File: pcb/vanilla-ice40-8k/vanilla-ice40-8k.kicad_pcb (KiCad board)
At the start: 6 copper layers, 50 x 50 mm, 129 parts, among them J10 Conn_01x05_Pin, J11 QSH-060-01-L-D-A, J12 QSH-060-01-L-D-A, J6 Conn_01x02_Pin, J7 Conn_01x02_Pin, J8 Conn_01x02_Pin, J9 Conn_01x06_Pin, Q1 DMG2305UX-13, U1 ICE40HX8K-CT256, U2 W25X40CLSN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

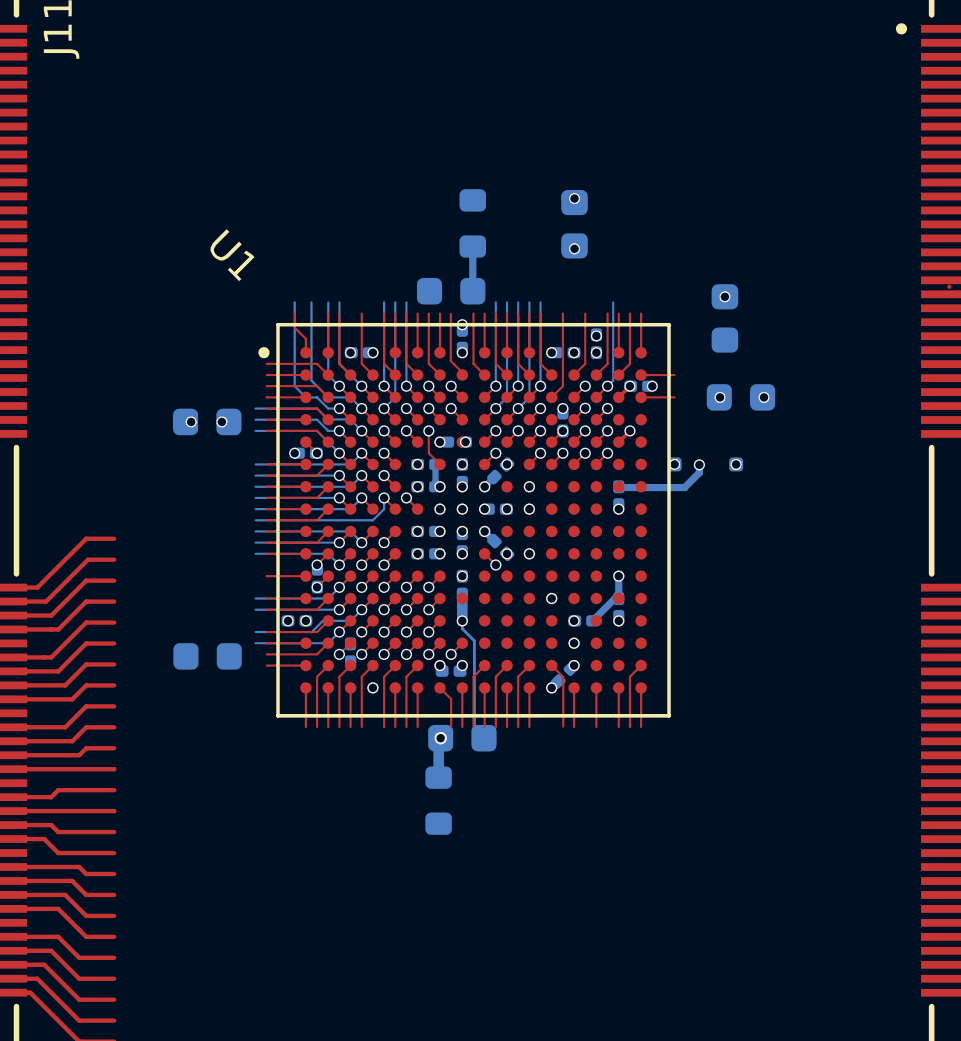
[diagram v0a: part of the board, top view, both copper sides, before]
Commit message: [pcb][hx8k] new IOR escape
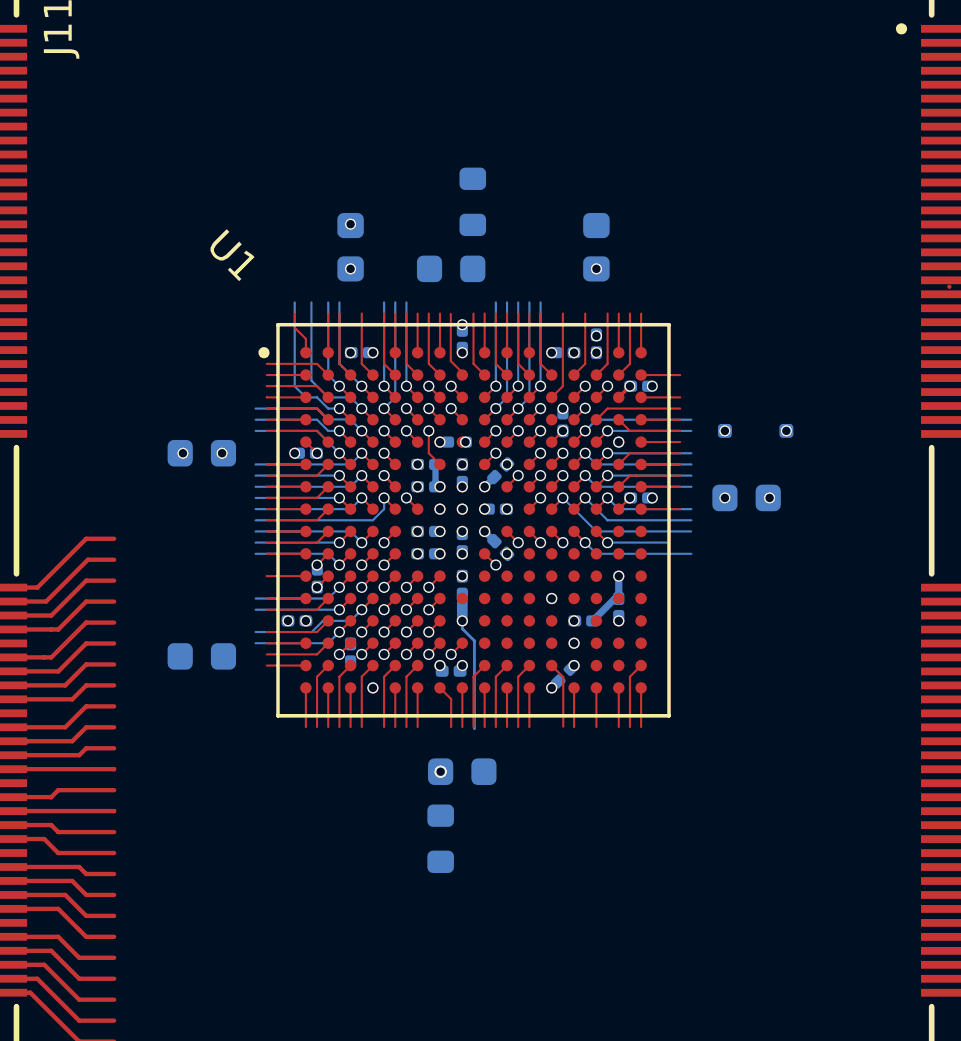
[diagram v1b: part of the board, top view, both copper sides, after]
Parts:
- moved C20 8.06 mm to (113.3, 105.4)
- moved C2 5.26 mm to (122.1, 105.4)
- moved C30 3.61 mm to (127.4, 114.4)
- moved D1 2.16 mm to (127.8, 112.0)
- moved R10 1.36 mm to (116.5, 126.6)
- moved C10 1.20 mm to (117.3, 124.2)
- moved C25 1.14 mm to (107.9, 112.8)
- moved C12 0.80 mm to (116.9, 106.2)
- moved R11 0.77 mm to (117.6, 103.8)
- moved C33 0.75 mm to (123.6, 114.4), turned to 0 degrees
- moved C15 0.21 mm to (107.9, 120.0)
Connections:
- U1 pad K11: unconnected-(U1C-IOB_103_CBSEL0-PadK11) -> /IOB_103_CBSEL0
- U1 pad P13: unconnected-(U1C-IOB_104_CBSEL1-PadP13) -> /IOB_103_CBSEL1
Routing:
- net /IOR_146_SCL: track 36.1 -> 43.9 mm, vias 1 -> 2
- net /IOR_158: track 0.57 -> 6.72 mm
- net /IOR_140_USR1: track 18.3 -> 24.4 mm
- net /IOR_148_SCA: track 37.1 -> 43.0 mm
- net /IOR_144: track 0.00 -> 5.65 mm, vias 0 -> 1
- net /IOR_154_USR2: track 16.2 -> 21.3 mm, vias 1 -> 2
- net /IOR_156: track 0.57 -> 5.67 mm
- net /IOR_139: track 0.00 -> 4.70 mm, vias 0 -> 1
- net /IOR_152: track 0.00 -> 4.53 mm, vias 0 -> 1
- net /IOR_137: track 0.00 -> 4.53 mm, vias 0 -> 1
- net /IOR_166: track 0.57 -> 4.53 mm
- net /IOR_162: track 0.57 -> 4.53 mm
- net GND: track 47.2 -> 43.2 mm, vias 175 -> 174
- net /IOR_142: track 0.00 -> 3.73 mm, vias 0 -> 1
- net /IOR_150: track 0.00 -> 3.57 mm, vias 0 -> 1
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
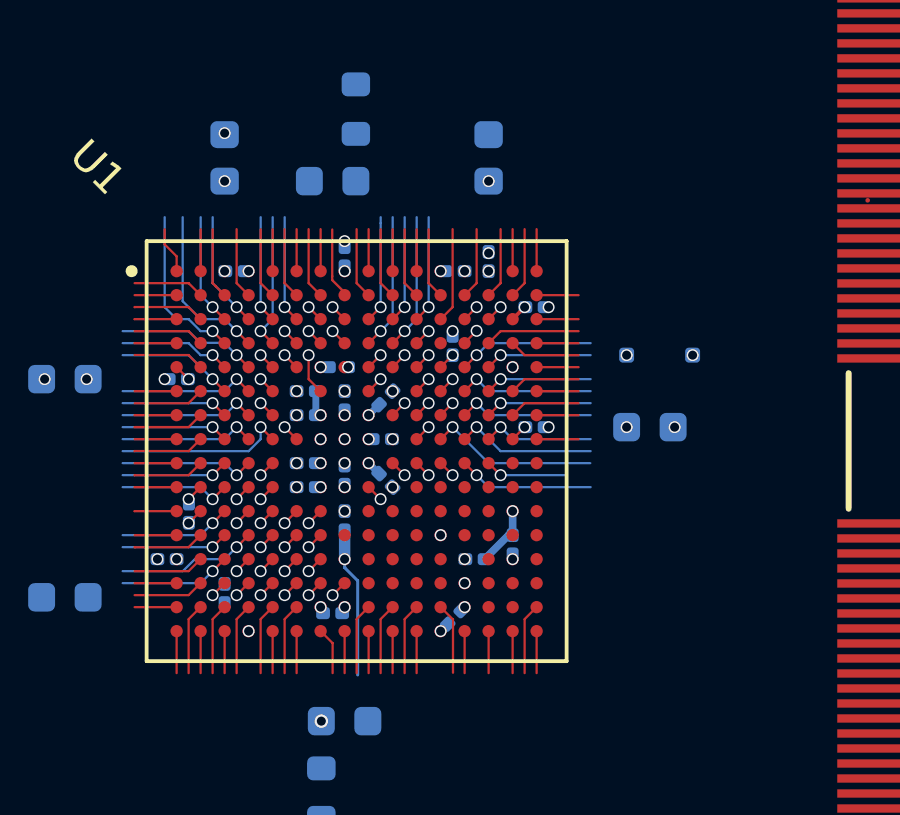
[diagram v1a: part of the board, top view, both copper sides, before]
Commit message: [pcb][hx8k] better IOR routing
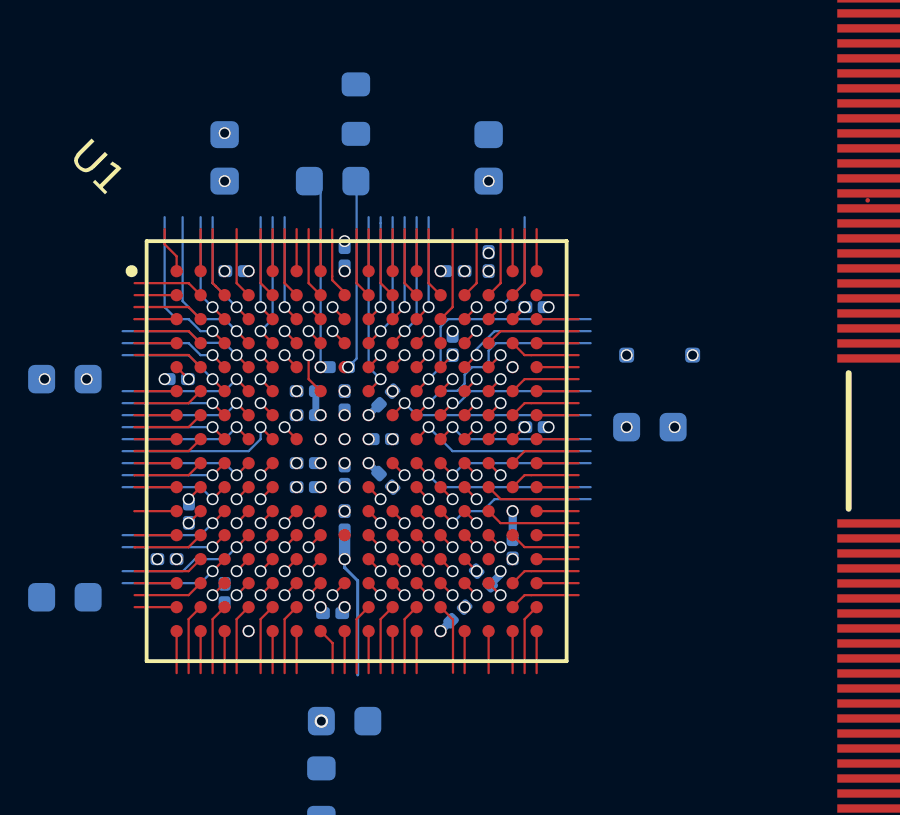
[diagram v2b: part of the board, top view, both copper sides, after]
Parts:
- moved C14 0.69 mm to (121.9, 119.4), turned to -45 degrees
- moved C18 0.16 mm to (121.0, 120.6)
- moved C34 0.14 mm to (122.9, 118.4)
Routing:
- net /hx8k power/GNDPLL1: track 0.00 -> 6.63 mm
- net /IOR_122_BUT1: track 9.44 -> 15.8 mm
- net Net-(U1E-VCCPLL1): track 0.00 -> 6.33 mm
- net /IOR_126_UTX: track 1.40 -> 6.96 mm
- net /IOR_116: track 0.00 -> 5.50 mm, vias 0 -> 1
- net /IOR_120: track 0.00 -> 5.13 mm, vias 0 -> 1
- net /IOR_136_URX: track 7.41 -> 12.2 mm
- net /IOR_114: track 0.00 -> 4.33 mm, vias 0 -> 1
- net /IOR_128: track 0.00 -> 4.17 mm, vias 0 -> 1
- net /IOR_118: track 0.00 -> 4.17 mm, vias 0 -> 1
- net /IOR_115: track 0.00 -> 3.37 mm, vias 0 -> 1
- net /IOR_111: track 0.00 -> 3.37 mm, vias 0 -> 1
- net /IOR_129: track 0.00 -> 3.17 mm
- net /IOR_119: track 0.00 -> 3.17 mm
- net /IOR_131: track 0.00 -> 2.37 mm
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
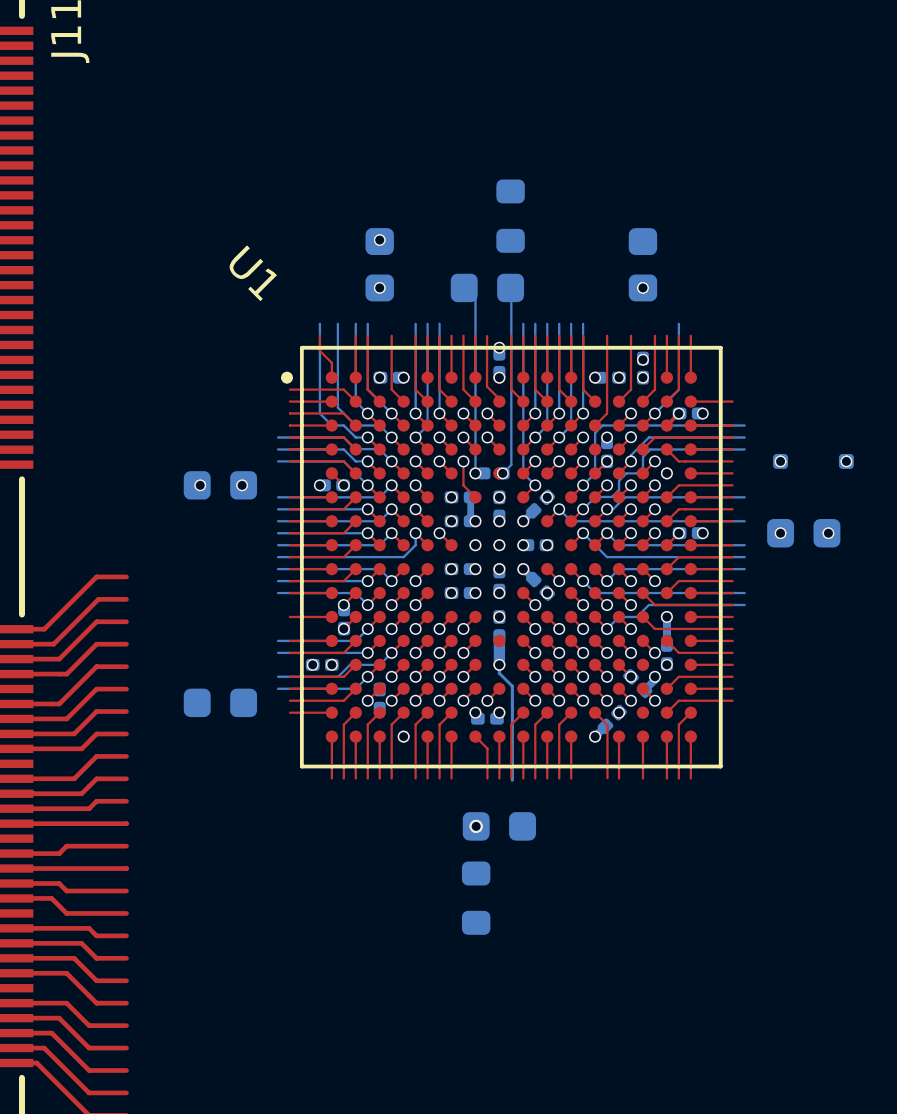
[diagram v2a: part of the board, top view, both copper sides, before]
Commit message: [pcb][hx8k] improve pll routing spearation
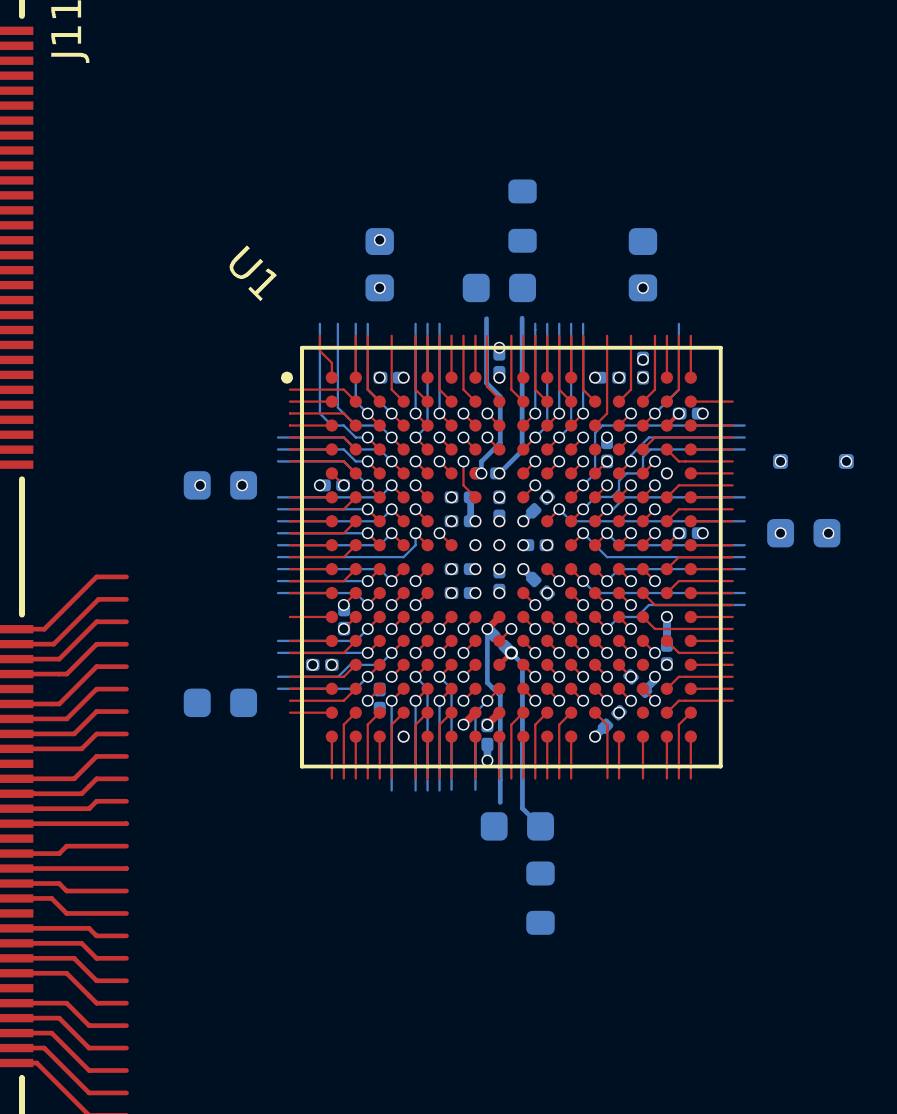
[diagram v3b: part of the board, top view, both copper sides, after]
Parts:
- moved R10 2.15 mm to (118.6, 126.6)
- moved C10 0.60 mm to (117.9, 124.2)
- moved C19 0.55 mm to (116.9, 121.1), turned to -90 degrees
- moved C9 0.48 mm to (117.3, 118.0), turned to -45 degrees
- moved C12 0.40 mm to (117.3, 106.2)
- moved R11 0.40 mm to (118.0, 103.8)
- moved C11 0.20 mm to (116.9, 112.4)
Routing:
- net Net-(U1E-VCCPLL0): track 0.15 -> 6.52 mm, vias 2 -> 1
- net /IOB_64: track 0.57 -> 5.55 mm
- net /IOB_66: track 0.57 -> 4.79 mm
- net /IOB_56: track 0.57 -> 4.53 mm
- net /IOB_52: track 0.57 -> 4.51 mm
- net /IOB_72: track 0.57 -> 3.71 mm
- net /IOB_67: track 0.57 -> 3.57 mm
- net /IOB_58: track 0.57 -> 3.57 mm
- net /IOB_54: track 0.57 -> 3.57 mm
- net /IOB_77: track 0.57 -> 3.33 mm
- net /IOT_196: track 6.13 -> 8.06 mm
- net /hx8k power/GNDPLL0: track 5.48 -> 6.77 mm
- net GND: track 44.3 -> 45.4 mm, vias 175 -> 176
- net /hx8k power/GNDPLL1: track 6.63 -> 5.70 mm
- net Net-(U1E-VCCPLL1): track 6.33 -> 5.50 mm
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
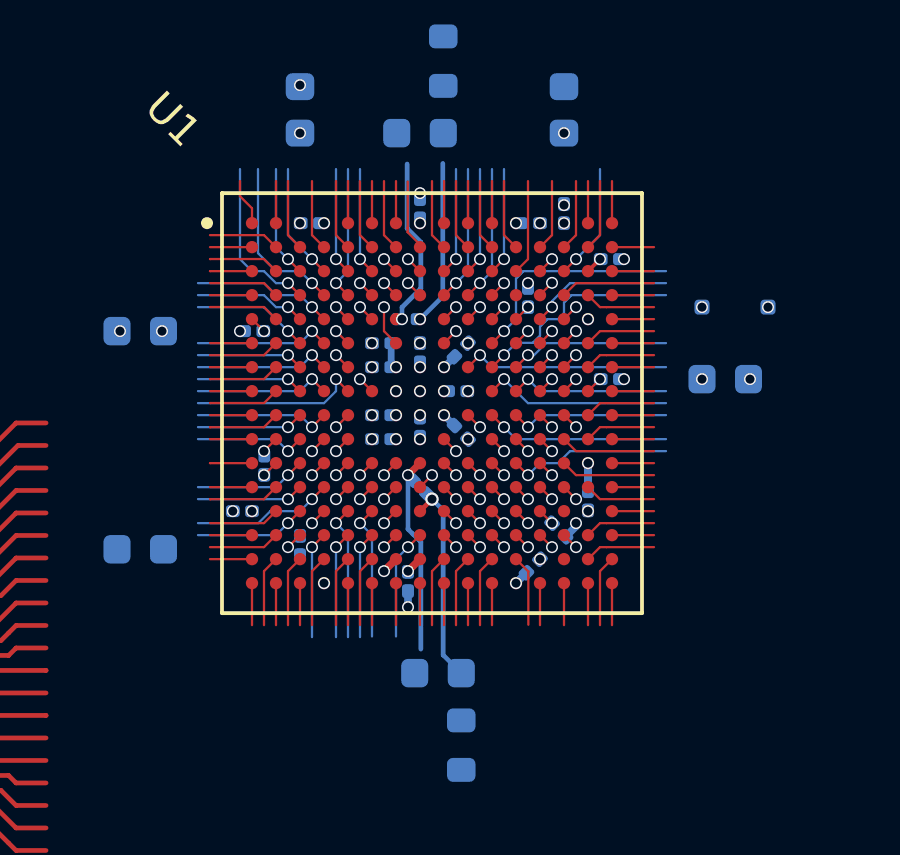
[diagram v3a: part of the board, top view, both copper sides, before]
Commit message: [pcb][hx8k] new escape done
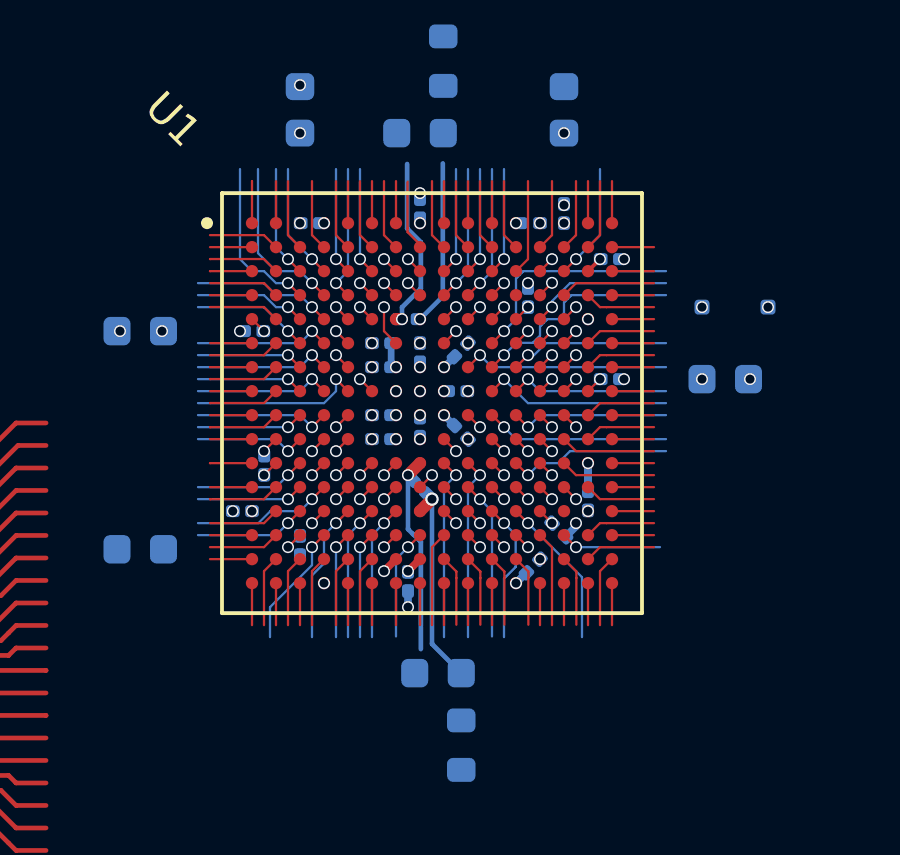
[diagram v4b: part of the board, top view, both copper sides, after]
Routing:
- net /IOB_82: track 0.57 -> 8.35 mm
- net /IOB_103_CBSEL0: track 0.57 -> 8.07 mm
- net /IOB_99: track 0.57 -> 6.61 mm
- net /IOB_101: track 0.57 -> 6.45 mm
- net /IOB_93: track 0.57 -> 6.38 mm
- net /IOB_68: track 0.57 -> 6.26 mm
- net /IOB_85: track 0.57 -> 6.13 mm
- net /IOB_74: track 0.57 -> 6.13 mm
- net /CDONE: track 25.4 -> 30.2 mm
- net /IOB_80: track 0.57 -> 5.15 mm
- net /IOB_98: track 0.57 -> 5.11 mm
- net /CRESET#: track 6.60 -> 10.7 mm
- net /IOB_87: track 0.57 -> 4.31 mm
- net /IOB_78: track 0.57 -> 4.17 mm
- net /IOB_86: track 0.57 -> 3.37 mm
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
